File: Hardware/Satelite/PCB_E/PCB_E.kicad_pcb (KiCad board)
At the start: 2 copper layers, 47 x 47 mm, 16 parts, among them J1 Conn_02x02_Counter_Clockwise, J10 Conn_02x04_Odd_Even, J11 Conn_02x04_Odd_Even, J12 Conector_Expansion_CanSat, J13 Conn_01x06, J14 Conn_01x06, J15 Conn_01x06, J2 Conn_02x02_Counter_Clockwise, J3 Conn_02x02_Counter_Clockwise, J4 Conn_02x04_Odd_Even, J5 Conn_02x04_Odd_Even, J6 Conn_02x04_Odd_Even, J7 Conn_02x04_Odd_Even, J8 Conn_02x04_Odd_Even, J9 Conn_02x04_Odd_Even

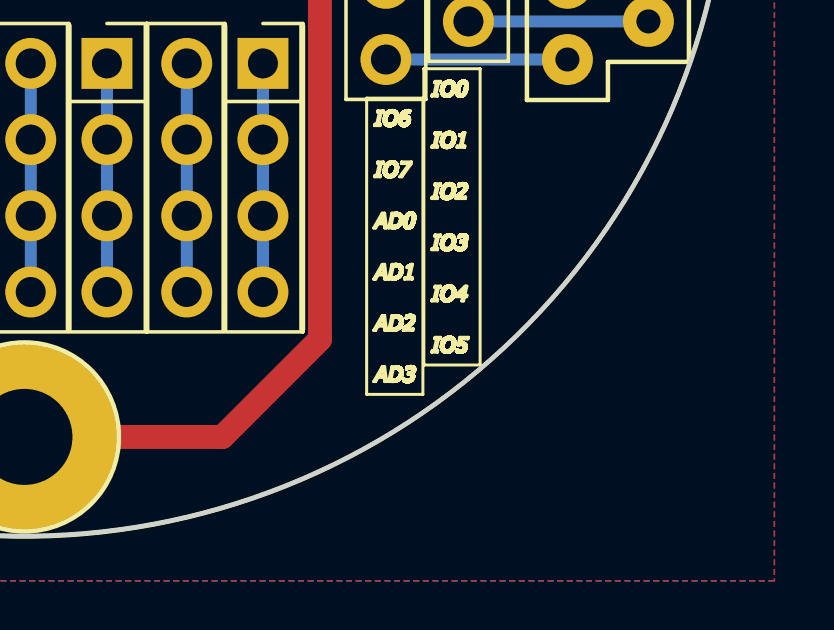
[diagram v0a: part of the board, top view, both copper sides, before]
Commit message: Corrección de serigrafía para conector de expansión
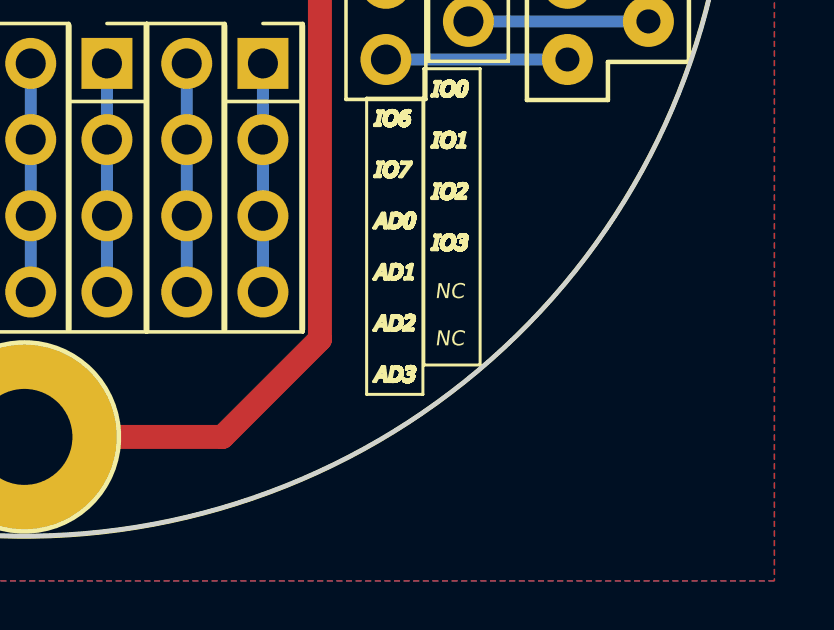
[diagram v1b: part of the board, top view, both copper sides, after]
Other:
- board text added: "NC"

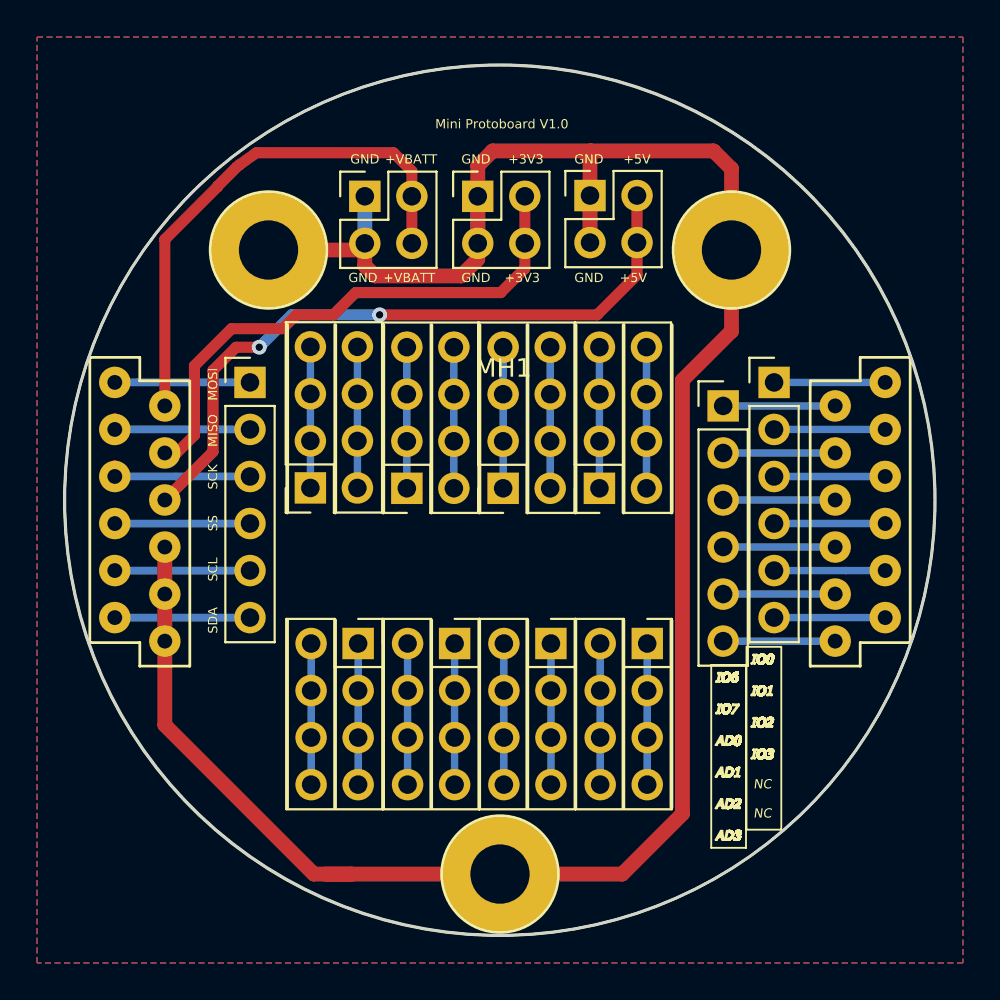
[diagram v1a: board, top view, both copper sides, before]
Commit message: Modificaciones en PCB_E y nuevas serigrafias
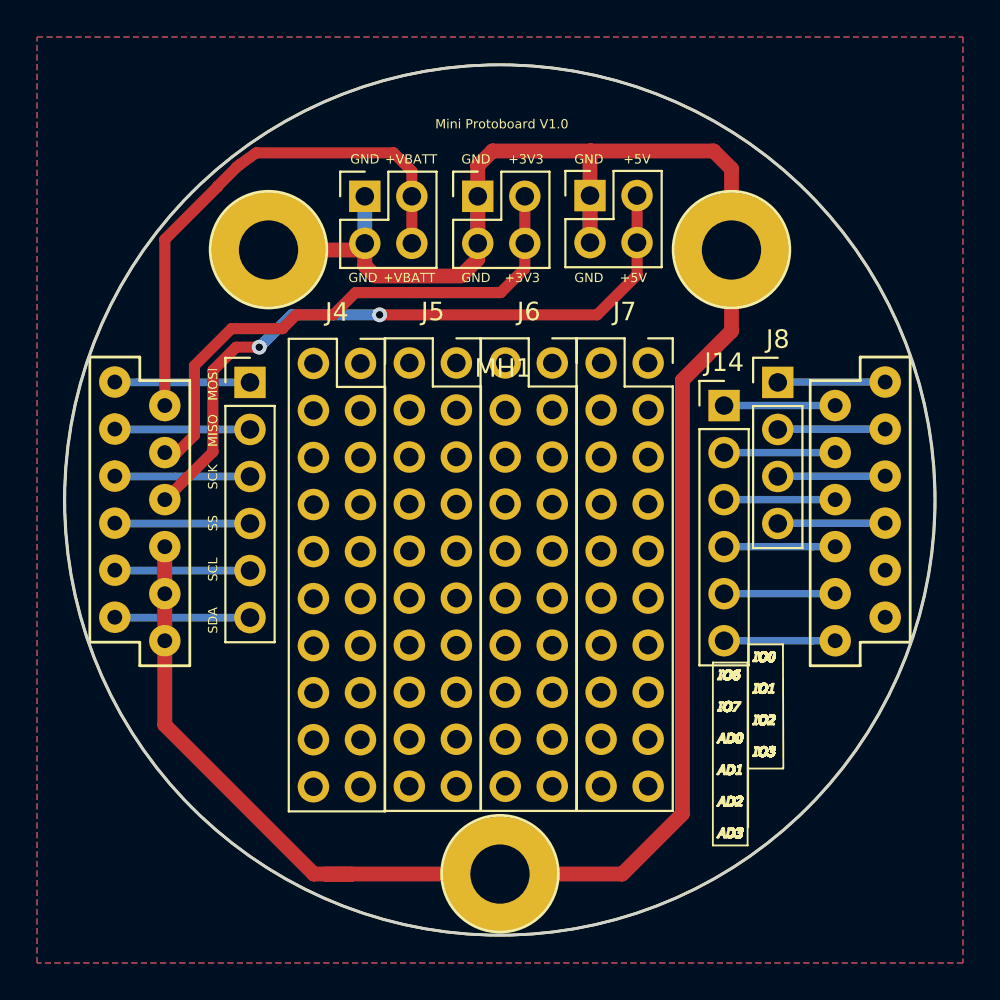
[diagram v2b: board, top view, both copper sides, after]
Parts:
- removed J10, J11, J9: Conn_02x04_Odd_Even, Connector_PinSocket_2.54mm:PinSocket_2x04_P2.54mm_Vertical
- removed J13: Conn_01x06, Connector_PinHeader_2.54mm:PinHeader_1x06_P2.54mm_Vertical
- added M1: Spacer, AXTEC:Empty_Footprint, F.Cu at (-4.75, -24.8)
- added M2: Spacer, AXTEC:Empty_Footprint, F.Cu at (-4.25, -24.8)
- added M3: Spacer, AXTEC:Empty_Footprint, F.Cu at (-3.75, -24.8)
- J4, J5, J6, J7: value Conn_02x04_Odd_Even -> Conn_02x10_Odd_Even; footprint Connector_PinSocket_2.54mm:PinSocket_2x04_P2.54mm_Vertical -> Connector_PinSocket_2.54mm:PinSocket_2x10_P2.54mm_Vertical
- J8: value Conn_02x04_Odd_Even -> Conn_01x04; footprint Connector_PinSocket_2.54mm:PinSocket_2x04_P2.54mm_Vertical -> Connector_PinHeader_2.54mm:PinHeader_1x04_P2.54mm_Vertical
- moved J8 18.7 mm to (15.0, -6.35)
- moved J6 16.0 mm to (2.82, -7.40)
- moved J7 10.3 mm to (8.00, -7.40), turned to 0 degrees
- moved J5 7.28 mm to (-2.36, -7.40), turned to 0 degrees
- moved J4 7.25 mm to (-7.53, -7.37), turned to 0 degrees
- moved J14 0.05 mm to (12.1, -5.10)
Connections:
- J4 pad 3: Net-(J4-Pad1) -> Net-(J4-Pad3)
- J4 pad 4: Net-(J4-Pad2) -> Net-(J4-Pad4)
- J4 pad 5: Net-(J4-Pad1) -> Net-(J4-Pad5)
- J4 pad 6: Net-(J4-Pad2) -> Net-(J4-Pad6)
- J4 pad 7: Net-(J4-Pad1) -> Net-(J4-Pad7)
- J4 pad 8: Net-(J4-Pad2) -> Net-(J4-Pad8)
- J5 pad 3: Net-(J5-Pad1) -> Net-(J5-Pad3)
- J5 pad 4: Net-(J5-Pad2) -> Net-(J5-Pad4)
- J5 pad 5: Net-(J5-Pad1) -> Net-(J5-Pad5)
- J5 pad 6: Net-(J5-Pad2) -> Net-(J5-Pad6)
- J5 pad 7: Net-(J5-Pad1) -> Net-(J5-Pad7)
- J5 pad 8: Net-(J5-Pad2) -> Net-(J5-Pad8)
- J6 pad 3: Net-(J6-Pad1) -> Net-(J6-Pad3)
- J6 pad 4: Net-(J6-Pad2) -> Net-(J6-Pad4)
- J6 pad 5: Net-(J6-Pad1) -> Net-(J6-Pad5)
- J6 pad 6: Net-(J6-Pad2) -> Net-(J6-Pad6)
- J6 pad 7: Net-(J6-Pad1) -> Net-(J6-Pad7)
- J6 pad 8: Net-(J6-Pad2) -> Net-(J6-Pad8)
- J7 pad 3: Net-(J7-Pad1) -> Net-(J7-Pad3)
- J7 pad 4: Net-(J7-Pad2) -> Net-(J7-Pad4)
- J7 pad 5: Net-(J7-Pad1) -> Net-(J7-Pad5)
- J7 pad 6: Net-(J7-Pad2) -> Net-(J7-Pad6)
- J7 pad 7: Net-(J7-Pad1) -> Net-(J7-Pad7)
- J7 pad 8: Net-(J7-Pad2) -> Net-(J7-Pad8)
- J8 pad 1: Net-(J8-Pad1) -> /IO0
- J8 pad 2: Net-(J8-Pad2) -> /IO1
- J8 pad 3: Net-(J8-Pad1) -> /IO2
- J8 pad 4: Net-(J8-Pad2) -> /IO3
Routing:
- net Net-(J9-Pad2): track 7.62 -> 0.00 mm
- net Net-(J9-Pad1): track 7.62 -> 0.00 mm
- net Net-(J7-Pad2): track 7.62 -> 0.00 mm
- net Net-(J7-Pad1): track 7.62 -> 0.00 mm
- net Net-(J5-Pad2): track 7.62 -> 0.00 mm
- net Net-(J5-Pad1): track 7.62 -> 0.00 mm
- net Net-(J8-Pad2): track 7.62 -> 0.00 mm
- net Net-(J8-Pad1): track 7.62 -> 0.00 mm
- net Net-(J6-Pad2): track 7.62 -> 0.00 mm
- net Net-(J6-Pad1): track 7.62 -> 0.00 mm
- net Net-(J4-Pad2): track 7.62 -> 0.00 mm
- net Net-(J4-Pad1): track 7.62 -> 0.00 mm
- net Net-(J11-Pad2): track 7.62 -> 0.00 mm
- net Net-(J11-Pad1): track 7.62 -> 0.00 mm
- net Net-(J10-Pad2): track 7.62 -> 0.00 mm
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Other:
- board text removed: "NC"
